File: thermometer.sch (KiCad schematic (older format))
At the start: 11 parts, among them IC1 ATTINY2313A-P, P1 CONN_4, P2 CONN_4, U1 MC78L05AACP

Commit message: Add C src
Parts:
- DD1: symbol Si705x -> Si705x-RESCUE-thermometer
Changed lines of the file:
@@
 EESchema Schematic File Version 2
+LIBS:thermometer-rescue
 LIBS:power
 LIBS:device
@@
 $EndDescr
 $Comp
-L Si705x DD1
+L Si705x-RESCUE-thermometer DD1
 U 1 1 57D7C352
 P 2050 3950

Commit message: Add I2C functions
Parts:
- added D1: LED, LEDs:LED-3MM, symbol LED
- added D2: max1555, TO_SOT_Packages_SMD:SOT-23-5, symbol max1555
- added P3: CONN_5, Connect:USB_Micro-B_10103594-0001LF, symbol CONN_5
- added R3: R, Resistors_ThroughHole:Resistor_Horizontal_RM10mm, symbol R
- DP1: footprint Socket_Strips:Socket_Strip_Straight_1x14 -> Socket_Strips:Socket_Strip_Angled_1x16
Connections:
- wire segments 73 -> 81
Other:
- moved on the sheet: BT1, C2

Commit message: Add
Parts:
- removed DD1: Si705x, Housings_DFN_QFN:DFN-6-1EP_3x3mm_Pitch0.95mm, symbol Si705x-RESCUE-thermometer
- removed DP1: LCD_Display, Socket_Strips:Socket_Strip_Angled_1x16, symbol LCD_Display
- added DD1: Si705x, Housings_DFN_QFN:DFN-6-1EP_3x3mm_Pitch0.95mm, symbol Si705x
- added DP1: LCD_Display_5, Socket_Strips:Socket_Strip_Angled_1x14, symbol LCD_Display_5
- added P4: CONN_4, Pin_Headers:Pin_Header_Straight_1x04, symbol CONN_4
- added R4, R5: 10k, Resistors_ThroughHole:Resistor_Horizontal_RM7mm, symbol R
- C2: footprint Capacitors_ThroughHole:C_Rect_L13_W4_P10 -> Capacitors_ThroughHole:C_Rect_L7_W2.5_P5
- R1, R2, R3: footprint Resistors_ThroughHole:Resistor_Horizontal_RM10mm -> Resistors_ThroughHole:Resistor_Horizontal_RM7mm
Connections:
- wire segments 81 -> 90

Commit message: Add ltc1517
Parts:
- removed U1: MC78L05AACP, TO_SOT_Packages_THT:TO-92_Rugged, symbol MC78L05AACP
- added C3: 6.8, Capacitors_ThroughHole:C_Radial_D5_L6_P2.5, symbol CP1
- added C4: 0.1, Capacitors_SMD:C_0805, symbol C
- added C5: 3.3, Capacitors_ThroughHole:C_Radial_D5_L6_P2.5, symbol CP1
- added DA1: LTC1517, TO_SOT_Packages_SMD:SOT-23-5, symbol LTC1517
- C2: value C -> 0.1
- R3: value R -> 330
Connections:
- wire segments 90 -> 99
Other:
- moved on the sheet: C2
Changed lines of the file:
@@
 LIBS:lcd_display
 LIBS:max1555
+LIBS:ltc1517
 LIBS:thermometer-cache
 EELAYER 25 0
@@
 L C C2
 U 1 1 57E3D673
-P 6050 1600
-F 0 "C2" H 6100 1700 50  0000 L CNN
-F 1 "C" H 6100 1500 50  0000 L CNN
-F 2 "Capacitors_ThroughHole:C_Rect_L7_W2.5_P5" H 6050 1600 60  0001 C CNN
-F 3 "" H 6050 1600 60  0000 C CNN
-	1    6050 1600
+P 5300 1600
+F 0 "C2" H 5350 1700 50  0000 L CNN
+F 1 "0.1" H 5350 1500 50  0000 L CNN
+F 2 "Capacitors_ThroughHole:C_Rect_L7_W2.5_P5" H 5300 1600 60  0001 C CNN
+F 3 "" H 5300 1600 60  0000 C CNN
+	1    5300 1600
 	1    0    0    -1
 $EndComp
@@
 L GNDPWR #PWR05
 U 1 1 57E3DDDE
-P 6050 1950
-F 0 "#PWR05" H 6050 2000 40  0001 C CNN
-F 1 "GNDPWR" H 6050 1870 40  0000 C CNN
-F 2 "" H 6050 1950 60  0000 C CNN
-F 3 "" H 6050 1950 60  0000 C CNN
-	1    6050 1950
+P 5300 1950
+F 0 "#PWR05" H 5300 2000 40  0001 C CNN
+F 1 "GNDPWR" H 5300 1870 40  0000 C CNN
+F 2 "" H 5300 1950 60  0000 C CNN
+F 3 "" H 5300 1950 60  0000 C CNN
+	1    5300 1950
 	1    0    0    -1
 $EndComp
@@
 L GNDPWR #PWR06
 U 1 1 57E3DE08
-P 6800 1950
-F 0 "#PWR06" H 6800 2000 40  0001 C CNN
-F 1 "GNDPWR" H 6800 1870 40  0000 C CNN
-F 2 "" H 6800 1950 60  0000 C CNN
-F 3 "" H 6800 1950 60  0000 C CNN
-	1    6800 1950
+P 6500 1950
+F 0 "#PWR06" H 6500 2000 40  0001 C CNN
+F 1 "GNDPWR" H 6500 1870 40  0000 C CNN
+F 2 "" H 6500 1950 60  0000 C CNN
+F 3 "" H 6500 1950 60  0000 C CNN
+	1    6500 1950
 	1    0    0    -1
 $EndComp
@@
 L VDD #PWR08
 U 1 1 57E3DE88
-P 6050 1150
-F 0 "#PWR08" H 6050 1250 30  0001 C CNN
-F 1 "VDD" H 6050 1260 30  0000 C CNN
-F 2 "" H 6050 1150 60  0000 C CNN
-F 3 "" H 6050 1150 60  0000 C CNN
-	1    6050 1150
-	1    0    0    -1
-$EndComp
-$Comp
-L MC78L05AACP U1
-U 1 1 57E3F03C
-P 6800 1250
-F 0 "U1" H 6600 1450 40  0000 C CNN
-F 1 "MC78L05AACP" H 6800 1450 40  0000 L CNN
-F 2 "TO_SOT_Packages_THT:TO-92_Rugged" H 6800 1350 30  0000 C CIN
-F 3 "" H 6800 1250 60  0000 C CNN
-	1    6800 1250
-	-1   0    0    -1
+P 5300 1150
+F 0 "#PWR08" H 5300 1250 30  0001 C CNN
+F 1 "VDD" H 5300 1260 30  0000 C CNN
+F 2 "" H 5300 1150 60  0000 C CNN
+F 3 "" H 5300 1150 60  0000 C CNN
+	1    5300 1150
+	1    0    0    -1
 $EndComp
 $Comp
@@
 P 7950 1600
 F 0 "R3" V 8030 1600 50  0000 C CNN
-F 1 "R" V 7950 1600 50  0000 C CNN
+F 1 "330" V 7950 1600 50  0000 C CNN
 F 2 "Resistors_ThroughHole:Resistor_Horizontal_RM7mm" H 7950 1600 60  0001 C CNN
 F 3 "" H 7950 1600 60  0000 C CNN
@@
 	5350 2600 5350 3750
 Wire Wire Line
-	7200 1200 8300 1200
+	6950 1200 8300 1200
 Wire Wire Line
 	7600 1200 7600 1300
 Wire Wire Line
-	6400 1200 6050 1200
-Wire Wire Line
-	6050 1150 6050 1400
-Connection ~ 6050 1200
-Wire Wire Line
-	6050 1800 6050 1950
-Wire Wire Line
-	6800 1500 6800 1950
+	5300 1200 6050 1200
+Wire Wire Line
+	5300 1150 5300 1400
+Connection ~ 5300 1200
+Wire Wire Line
+	5300 1800 5300 1950
+Wire Wire Line
+	6500 1600 6500 1950
 Wire Wire Line
 	7600 1900 7600 1950
@@
 	8900 4550 8500 4550
 Wire Wire Line
-	10450 3950 8500 3950
-Wire Wire Line
-	10450 4050 8500 4050
+	8500 3950 10450 3950
+Wire Wire Line
+	8500 4050 10450 4050
 Wire Wire Line
 	2750 3850 2550 3850
@@
 	10000 3750 10000 4050
 Connection ~ 10000 4050
+$Comp
+L LTC1517 DA1
+U 1 1 57F21D4C
+P 6500 1300
+F 0 "DA1" H 6700 1550 60  0000 C CNN
+F 1 "LTC1517" H 6300 1550 60  0000 C CNN
+F 2 "TO_SOT_Packages_SMD:SOT-23-5" H 6455 1715 60  0001 C CNN
+F 3 "" H 6455 1715 60  0000 C CNN
+	1    6500 1300
+	-1   0    0    -1
+$EndComp
+$Comp
+L CP1 C3
+U 1 1 57F222FE
+P 5600 1600
+F 0 "C3" H 5650 1700 50  0000 L CNN
+F 1 "6.8" H 5650 1500 50  0000 L CNN
+F 2 "Capacitors_ThroughHole:C_Radial_D5_L6_P2.5" H 5600 1600 60  0001 C CNN
+F 3 "" H 5600 1600 60  0000 C CNN
+	1    5600 1600
+	1    0    0    -1
+$EndComp
+$Comp
+L CP1 C5
+U 1 1 57F22365
+P 7200 1650
+F 0 "C5" H 7250 1750 50  0000 L CNN
+F 1 "3.3" H 7250 1550 50  0000 L CNN
+F 2 "Capacitors_ThroughHole:C_Radial_D5_L6_P2.5" H 7200 1650 60  0001 C CNN
+F 3 "" H 7200 1650 60  0000 C CNN
+	1    7200 1650
+	1    0    0    -1
+$EndComp
+$Comp
+L GNDPWR #PWR013
+U 1 1 57F2241A
+P 7200 1950
+F 0 "#PWR013" H 7200 2000 40  0001 C CNN
+F 1 "GNDPWR" H 7200 1870 40  0000 C CNN
+F 2 "" H 7200 1950 60  0000 C CNN
+F 3 "" H 7200 1950 60  0000 C CNN
+	1    7200 1950
+	1    0    0    -1
+$EndComp
+$Comp
+L GNDPWR #PWR014
+U 1 1 57F224CE
+P 5600 1950
+F 0 "#PWR014" H 5600 2000 40  0001 C CNN
+F 1 "GNDPWR" H 5600 1870 40  0000 C CNN
+F 2 "" H 5600 1950 60  0000 C CNN
+F 3 "" H 5600 1950 60  0000 C CNN
+	1    5600 1950
+	1    0    0    -1
+$EndComp
+Wire Wire Line
+	5600 1400 5600 1200
+Connection ~ 5600 1200
+Wire Wire Line
+	5600 1800 5600 1950
+Wire Wire Line
+	7200 1950 7200 1850
+Wire Wire Line
+	7200 1450 7200 1200
+Connection ~ 7200 1200
+$Comp
+L C C4
+U 1 1 57F2271C
+P 5950 1600
+F 0 "C4" H 6000 1700 50  0000 L CNN
+F 1 "0.1" H 6000 1500 50  0000 L CNN
+F 2 "Capacitors_SMD:C_0805" H 5950 1600 60  0001 C CNN
+F 3 "" H 5950 1600 60  0000 C CNN
+	1    5950 1600
+	-1   0    0    1
+$EndComp
+Wire Wire Line
+	6050 1300 5950 1300
+Wire Wire Line
+	5950 1300 5950 1400
+Wire Wire Line
+	5950 1800 7050 1800
+Wire Wire Line
+	7050 1800 7050 1300
+Wire Wire Line
+	7050 1300 6950 1300
 $EndSCHEMATC

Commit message: Fix Display
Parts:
- removed DA1: LTC1517, TO_SOT_Packages_SMD:SOT-23-5, symbol LTC1517
- removed P3: CONN_5, Connect:USB_Micro-B_10103594-0001LF, symbol CONN_5
- added DA1: LDK120, TO_SOT_Packages_SMD:SOT-23-5, symbol LDK120
- added P3: CONN_6, Connect:USB_Micro-B_10103594-0001LF, symbol CONN_6
- C3: value 6.8 -> 1.0
- C5: value 3.3 -> 1.0
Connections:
- wire segments 99 -> 102
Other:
- moved on the sheet: C4, P4

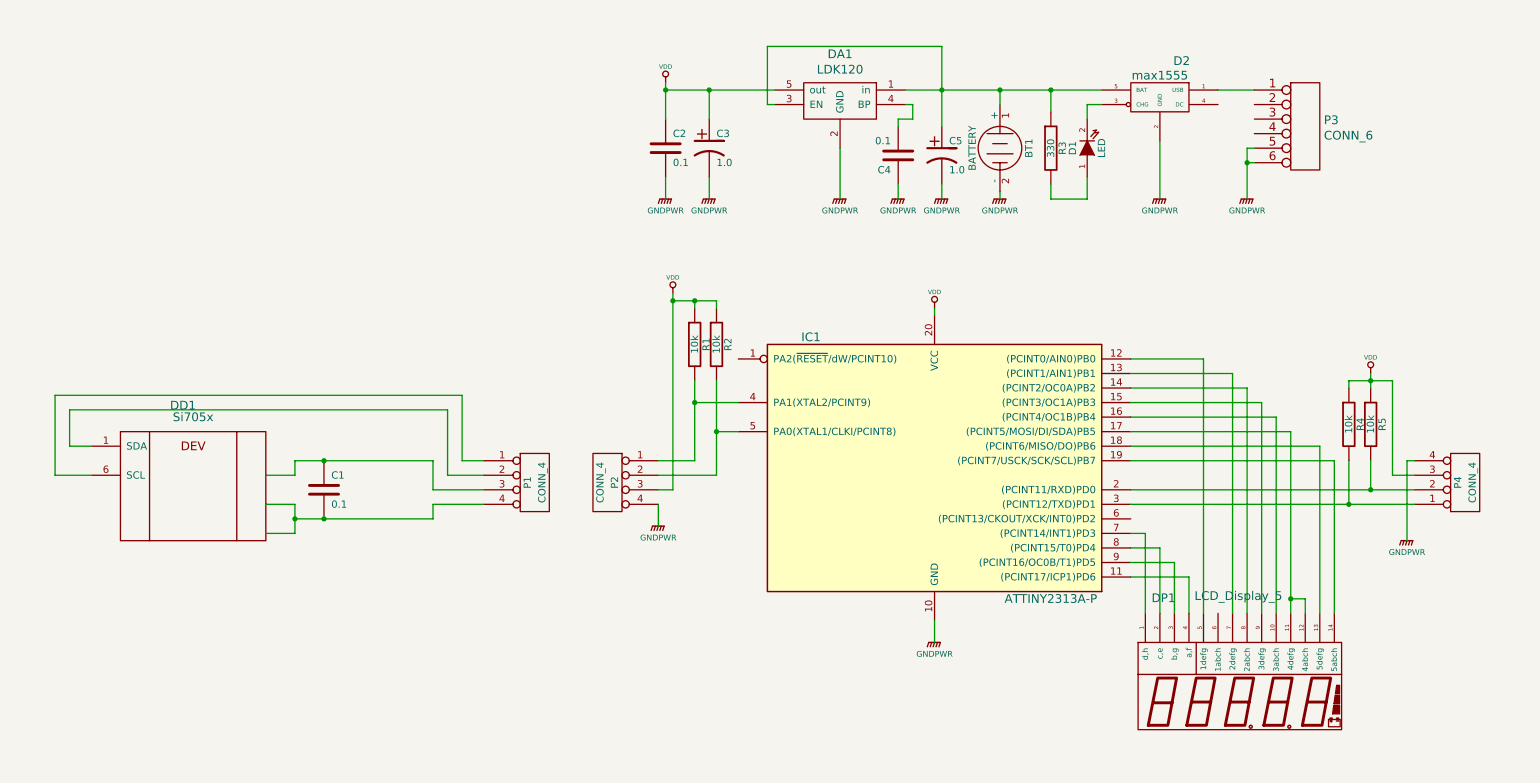
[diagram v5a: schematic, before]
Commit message: Add power supply for temperature sensor.
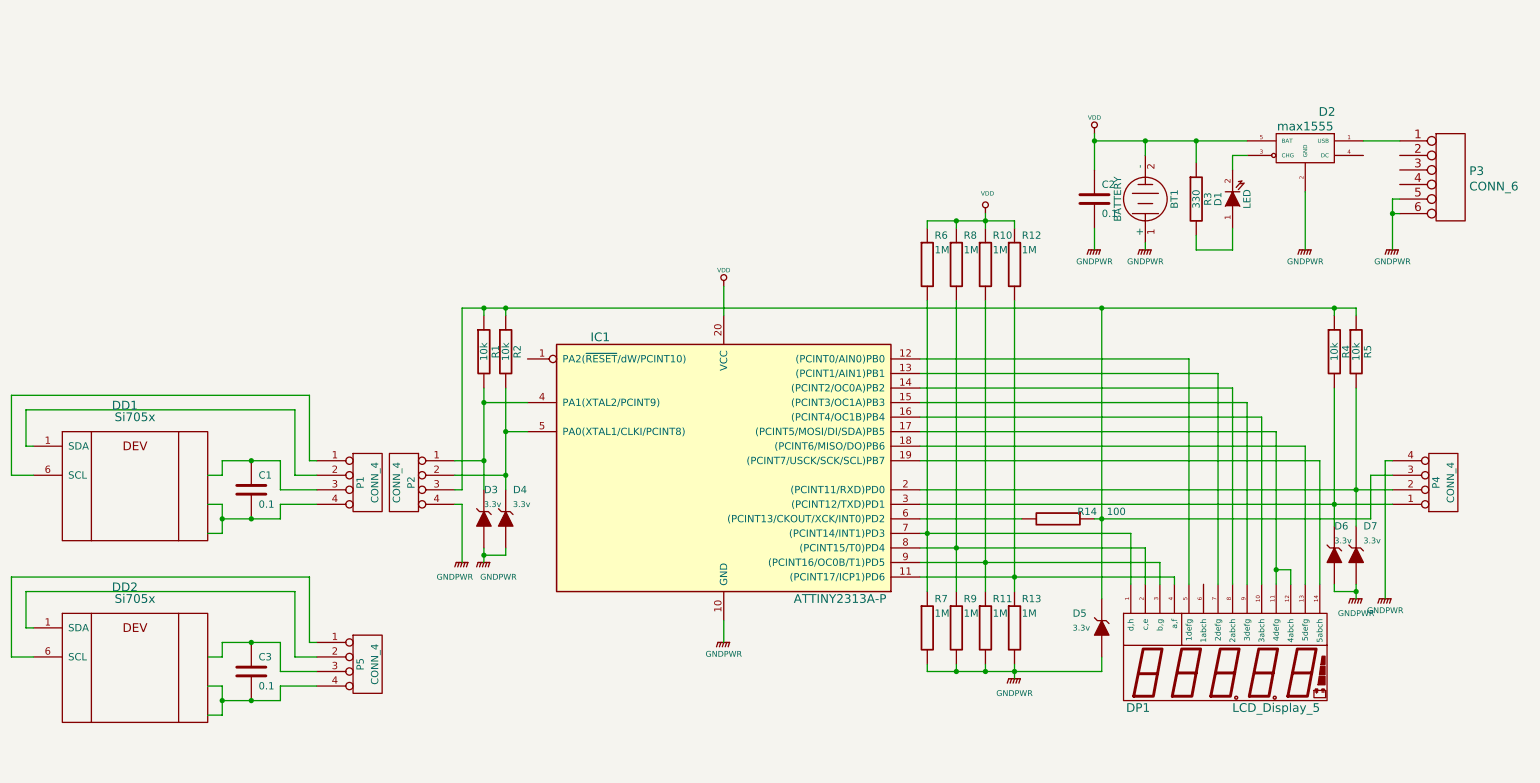
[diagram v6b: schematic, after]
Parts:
- removed C3, C5: 1.0, Capacitors_ThroughHole:C_Radial_D5_L6_P2.5, symbol CP1
- removed C4: 0.1, Capacitors_SMD:C_0805, symbol C
- removed DA1: LDK120, TO_SOT_Packages_SMD:SOT-23-5, symbol LDK120
- added C3: 0.1, Capacitors_SMD:C_0805, symbol C
- added D3, D4, D5, D6, D7: 3.3v, Diodes_SMD:MELF_Standard, symbol ZENER
- added DD2: Si705x, Housings_DFN_QFN:DFN-6-1EP_3x3mm_Pitch0.95mm, symbol Si705x
- added P5: CONN_4, Pin_Headers:Pin_Header_Straight_2x02, symbol CONN_4
- added R10, R11, R12, R13, R6, R7, R8, R9: 1M, Resistors_SMD:R_0805, symbol R
- added R14: 100, Resistors_SMD:R_0805, symbol R
- C2: footprint Capacitors_ThroughHole:C_Rect_L7_W2.5_P5 -> Capacitors_SMD:C_0805
- R3: footprint Resistors_ThroughHole:Resistor_Horizontal_RM7mm -> Resistors_SMD:R_0805
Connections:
- net GND: now also C3.2, DD2.2 (GND), DD2.7 (GND), P5.4 (P4)
- net GNDPWR: now also BT1.1 (+), D3.1 (A), D4.1 (A), D5.1 (A), D6.1 (A), D7.1 (A), R11.2, R13.2, R7.2, R9.2; no longer BT1.2 (-)
- net NC: now also DD2.3 (NC), DD2.4 (NC)
- net VCC: now also C3.1, DD2.5 (VCC), P5.3 (P3)
- net VDD: now also BT1.2 (-), D2.5 (BAT), R3.1, R10.1, R12.1, R6.1, R8.1; no longer P2.3 (P3), P4.3 (P3), R1.1, R2.1, R4.1, R5.1
- net at IC1.5 (PA0(XTAL1/CLKI/PCINT8)), P2.2 (P2), R2.2: now also D4.2 (K)
- net at IC1.4 (PA1(XTAL2/PCINT9)), P2.1 (P1), R1.2: now also D3.2 (K)
- net at DP1.4 (a,f), IC1.11 ((PCINT17/ICP1)PD6): now also R12.2, R13.1
- net at IC1.2 ((PCINT11/RXD)PD0), P4.2 (P2), R5.2: now also D7.2 (K)
- net at IC1.3 ((PCINT12/TXD)PD1), P4.1 (P1), R4.2: now also D6.2 (K)
- net at IC1.6 ((PCINT13/CKOUT/XCK/INT0)PD2): now also R14.2
- net at DP1.1 (d,h), IC1.7 ((PCINT14/INT1)PD3): now also R6.2, R7.1
- net at DP1.2 (c,e), IC1.8 ((PCINT15/T0)PD4): now also R8.2, R9.1
- net at DP1.3 (b,g), IC1.9 ((PCINT16/OC0B/T1)PD5): now also R10.2, R11.1
- new net: D5.2 (K), P2.3 (P3), P4.3 (P3), R1.1, R14.1, R2.1, R4.1, R5.1
- new net: DD2.6 (SCL), P5.1 (P1)
- new net: DD2.1 (SDA), P5.2 (P2)
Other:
- moved on the sheet: BT1, C1, C2, D1, D2, DD1, DP1, IC1, P1, P2, P3, P4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

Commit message: Fixes
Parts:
- BT1: symbol BATTERY -> thermometer-rescue:BATTERY
- C1, C2, C3: symbol C -> thermometer-rescue:C
- D1: symbol LED -> thermometer-rescue:LED
- D2: symbol max1555 -> lcd_display:max1555
- D3, D4, D5, D6, D7: symbol ZENER -> thermometer-rescue:ZENER
- DD1, DD2: symbol Si705x -> si705x:Si705x
- DP1: symbol LCD_Display_5 -> lcd_display:LCD_Display_5
- IC1: symbol ATTINY2313A-P -> thermometer-rescue:ATTINY2313A-P
- P1, P2, P4, P5: symbol CONN_4 -> thermometer-rescue:CONN_4
- P3: symbol CONN_6 -> thermometer-rescue:CONN_6
- R1, R10, R11, R12, R13, R14, R2, R3, R4, R5, R6, R7, R8, R9: symbol R -> thermometer-rescue:R
